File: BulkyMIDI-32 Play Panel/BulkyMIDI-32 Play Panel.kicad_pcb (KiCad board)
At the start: 2 copper layers, 100 x 23.2 mm, 11 parts, among them IC1 0.91_I2C_OLED, J1 Play_Panel, M1 Mounting_Pin, M2 Mounting_Pin, M3 Mounting_Pin, M4 Mounting_Pin

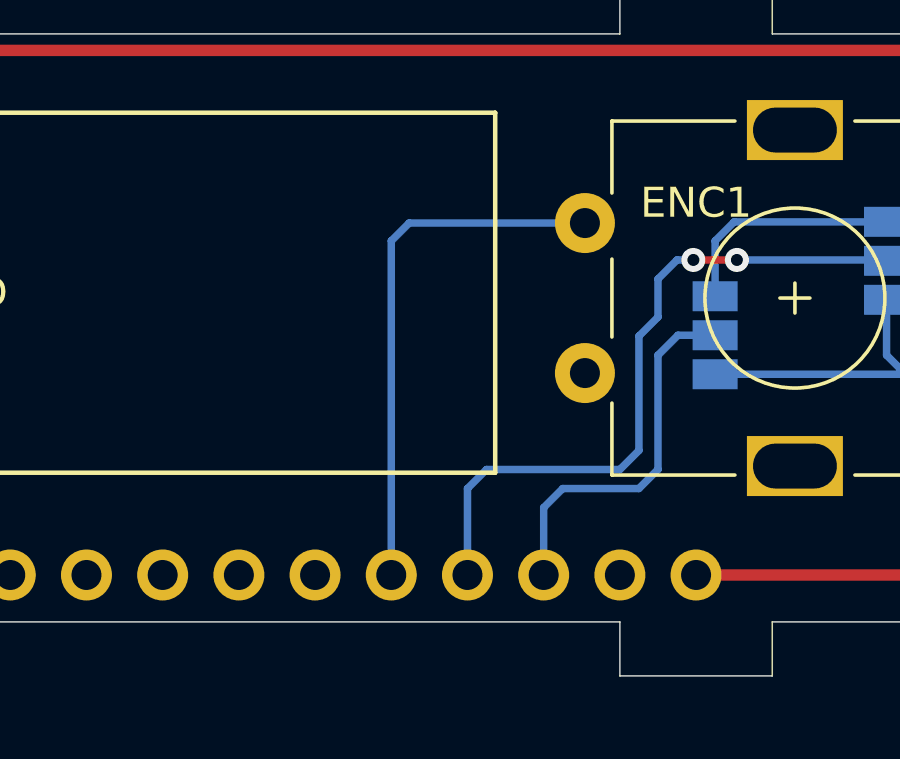
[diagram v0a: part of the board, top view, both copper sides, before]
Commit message: Added Play FP1 and a post for holding OLED
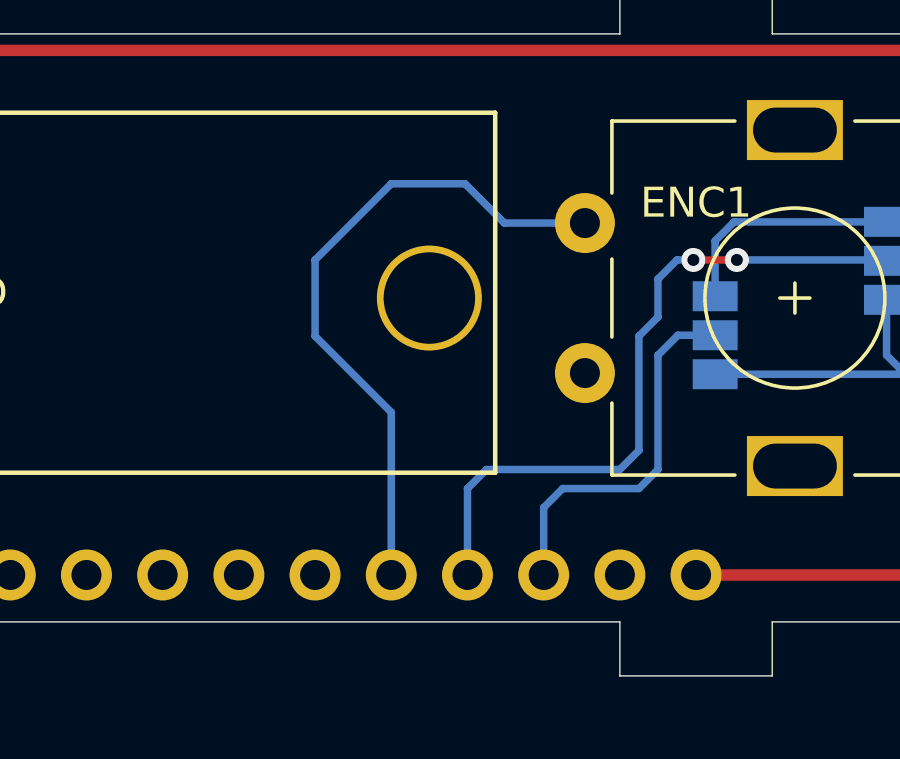
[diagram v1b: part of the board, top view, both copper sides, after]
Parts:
- added M5: Mounting_Pin, mounting:M3_pin, F.Cu at (157.6, 121.6)
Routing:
- net /BTN: track 17.8 -> 22.1 mm

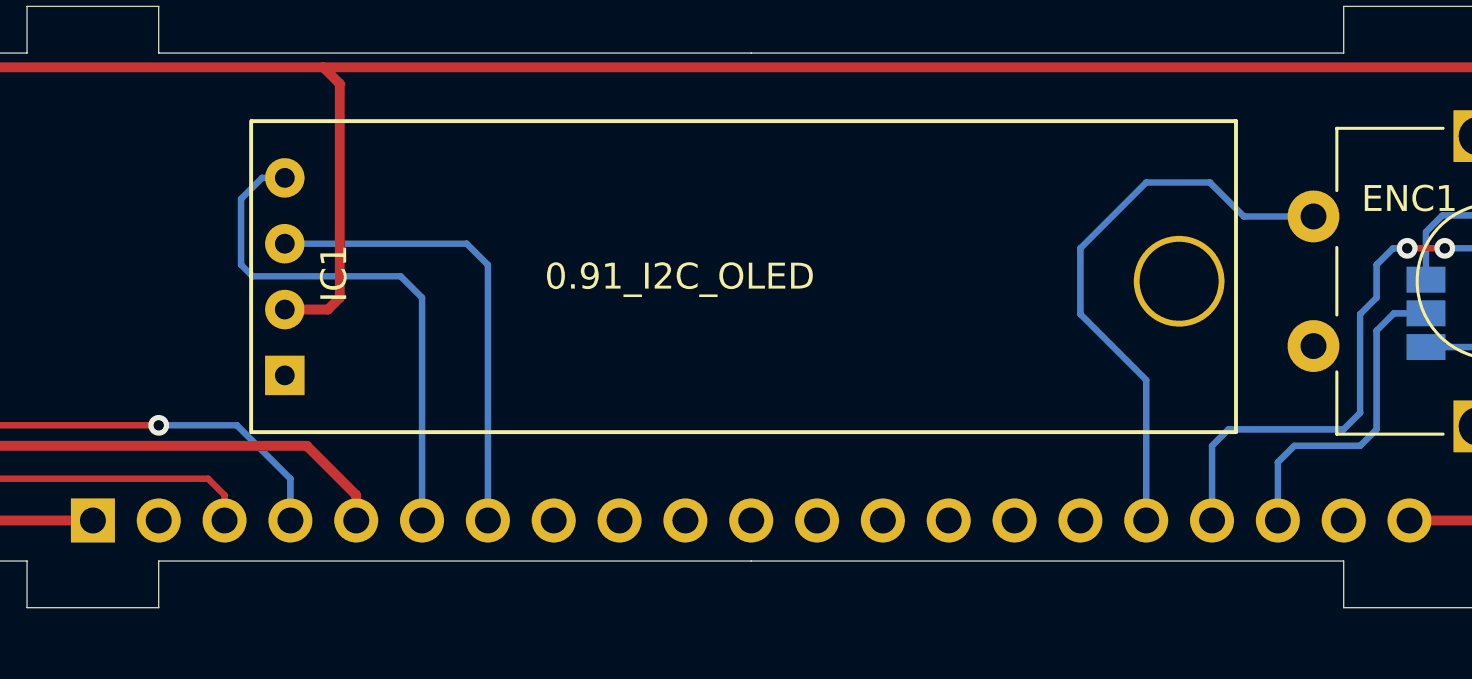
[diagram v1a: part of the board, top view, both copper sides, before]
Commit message: Updated display footprint
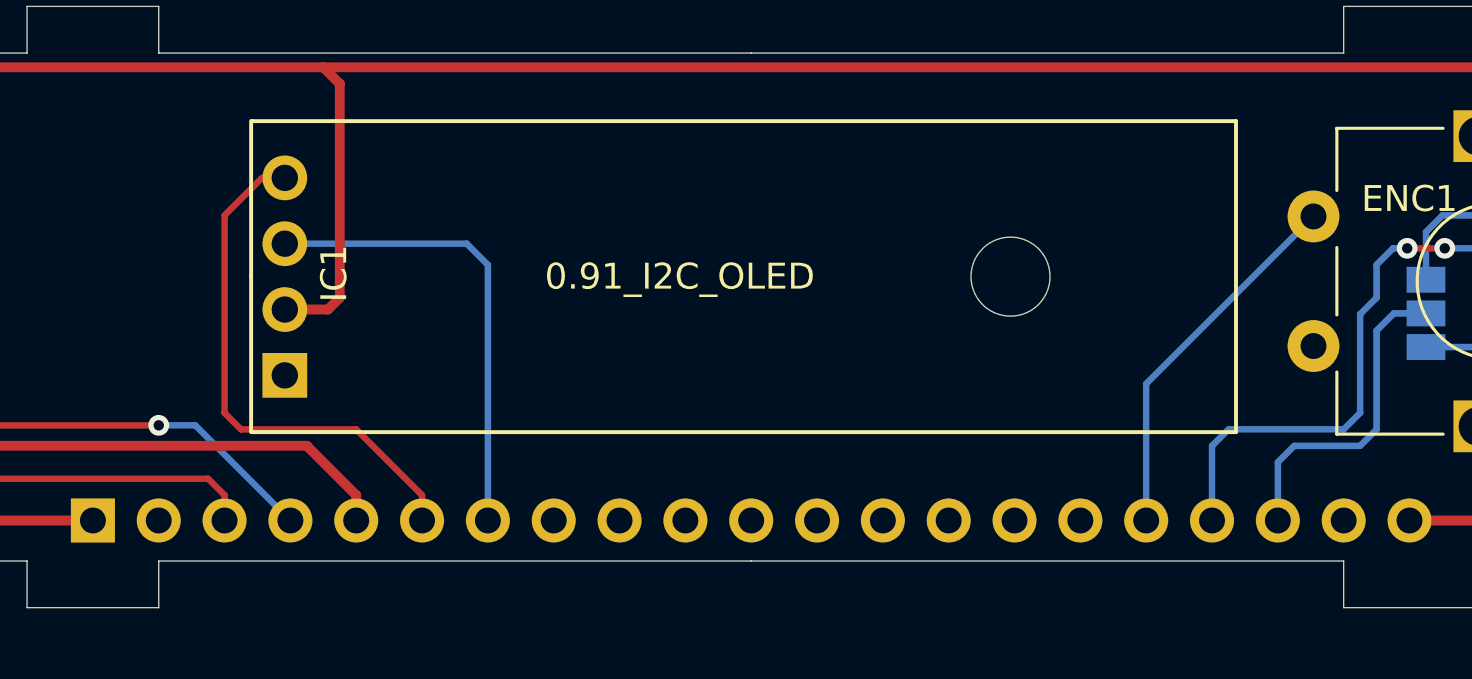
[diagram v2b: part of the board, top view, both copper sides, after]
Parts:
- removed M5: Mounting_Pin, mounting:M3_pin
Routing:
- net /BTN: track 22.1 -> 14.4 mm
- net /ACT: track 24.5 -> 23.6 mm
